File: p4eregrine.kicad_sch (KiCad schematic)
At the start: 44 parts, among them U1 ESP32-P4NRW32X, U15 TPD2EUSB30A, U3 W25Q128JVP, U7 GT-USB-7079C, Y1 Crystal_GND24

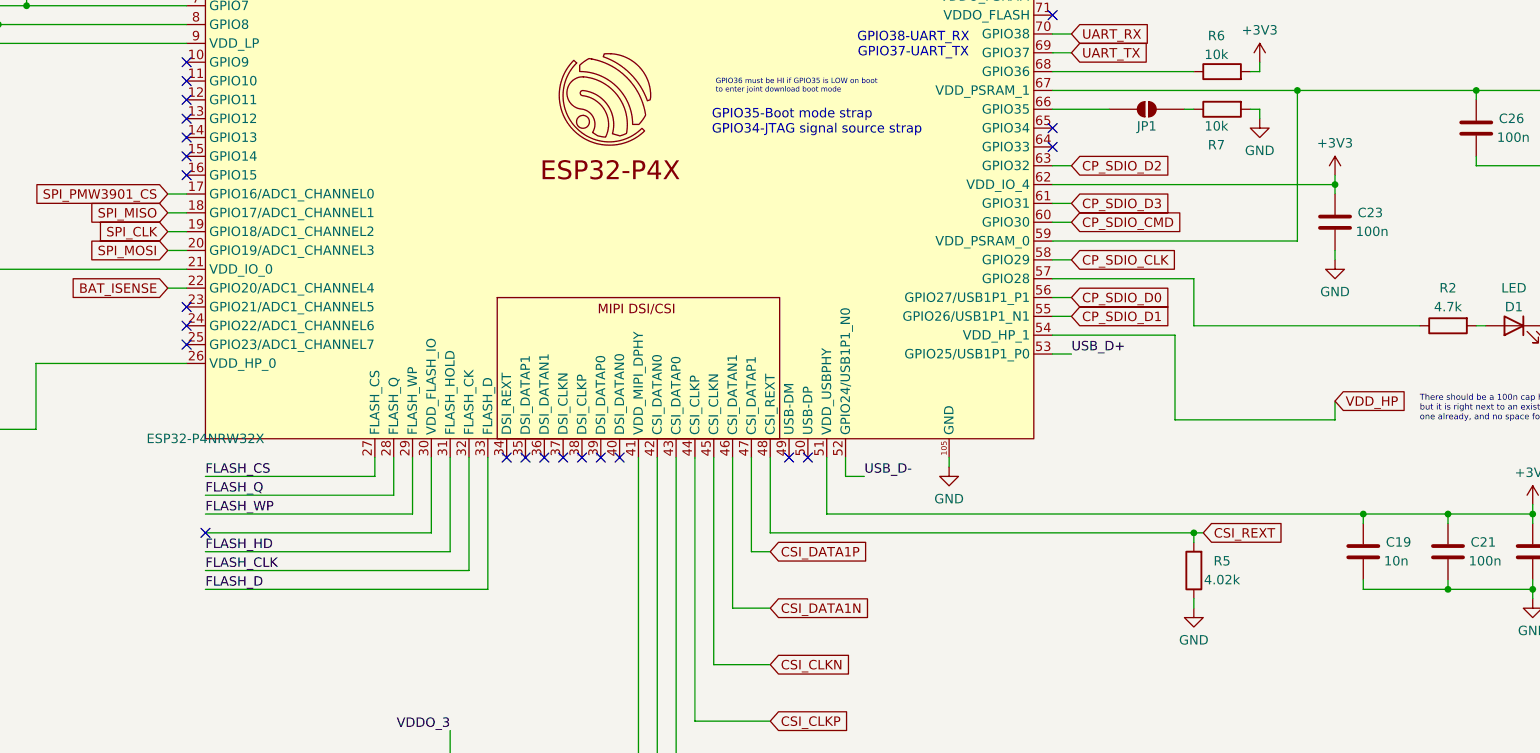
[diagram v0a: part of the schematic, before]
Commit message: Rename project
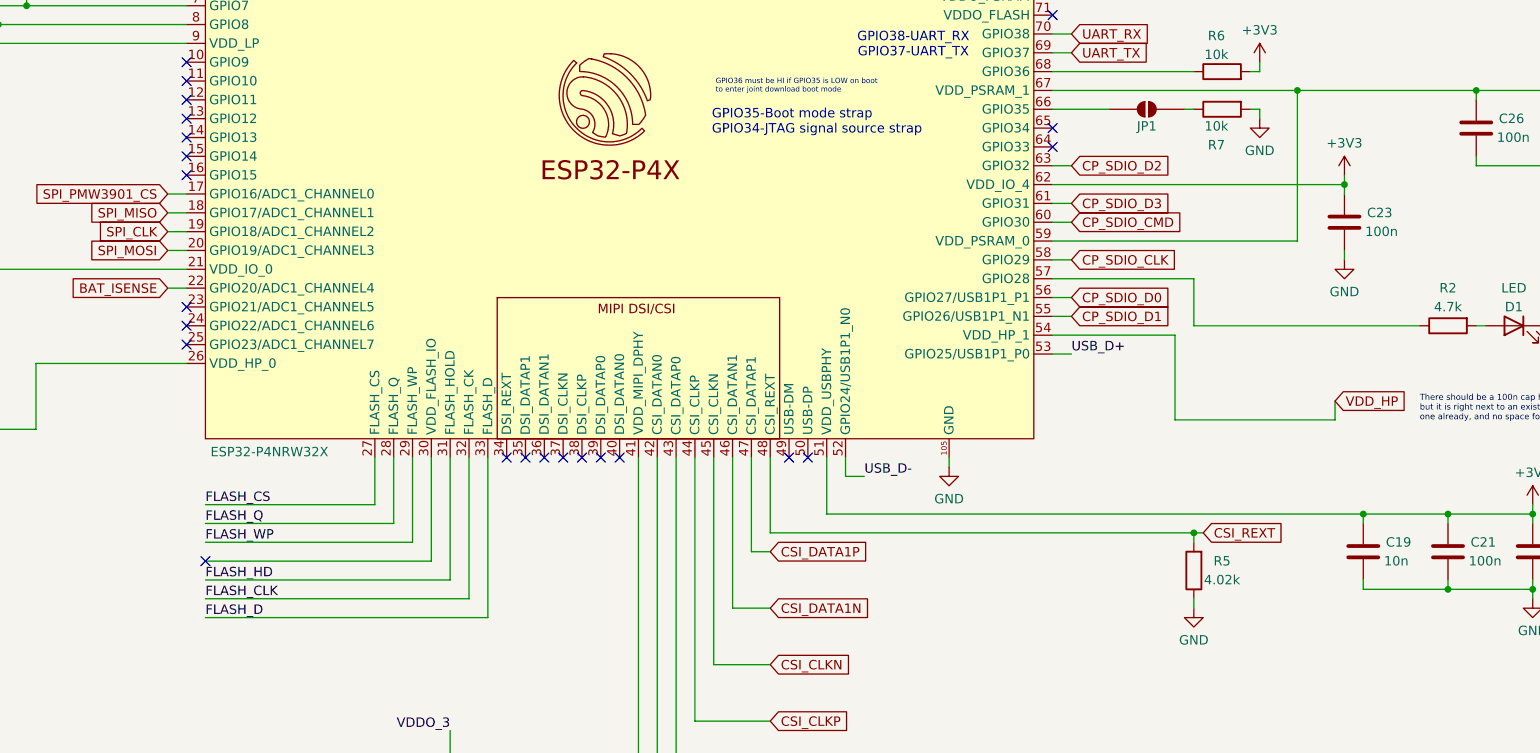
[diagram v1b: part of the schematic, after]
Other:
- title: Anticopter Duo -> P4eregrine
- moved on the sheet: C23

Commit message: Improve silkscreen and ground pour via stitching
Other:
- note added: "MIPI PHY supply"
- note added: "PMW3901B 2.1V supply"
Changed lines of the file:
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@@
+		)
+	)
+	(text "PMW3901B 2.1V supply"
+		(exclude_from_sim no)
+		(at 308.356 138.684 0)
+		(effects
+			(font
+				(size 1.27 1.27)
+			)
 		)
 	)
@@
 		(effects
 			(font
+				(size 1.27 1.27)
+			)
+		)
+	)
+	(text "MIPI PHY supply"
+		(exclude_from_sim no)
+		(at 282.702 138.176 0)
+		(effects
+			(font

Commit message: Add power supply comments to schematic
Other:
- note added: "Using 4.7k resistors to minimize BOM which is still within USB-C specs"
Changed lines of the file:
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@@
+		)
+	)
+	(text "Using 4.7k resistors to minimize BOM\nwhich is still within USB-C specs"
+		(exclude_from_sim no)
+		(at 261.112 84.074 0)
+		(effects
+			(font
+				(size 1.27 1.27)
+			)
+			(justify left)
 		)
 	)

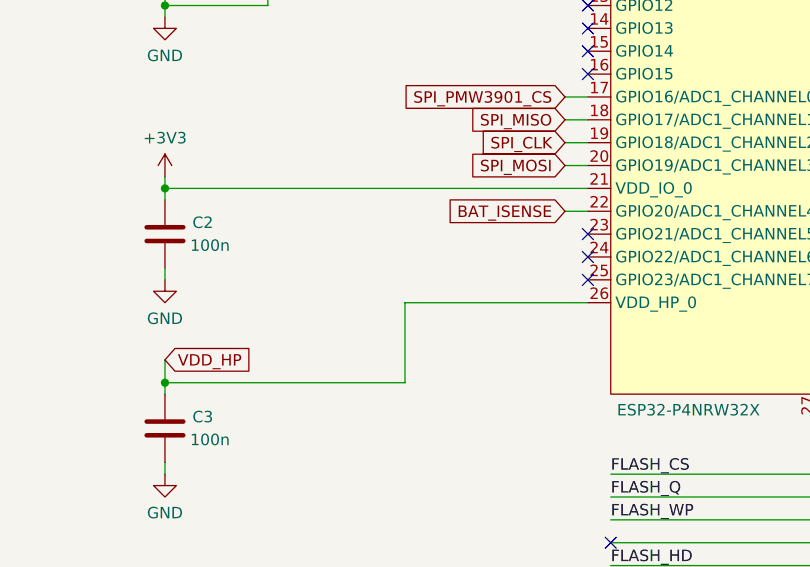
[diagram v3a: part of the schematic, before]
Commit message: Add BAT_ISENSE filtering cap and improve 3v3 plane continuity
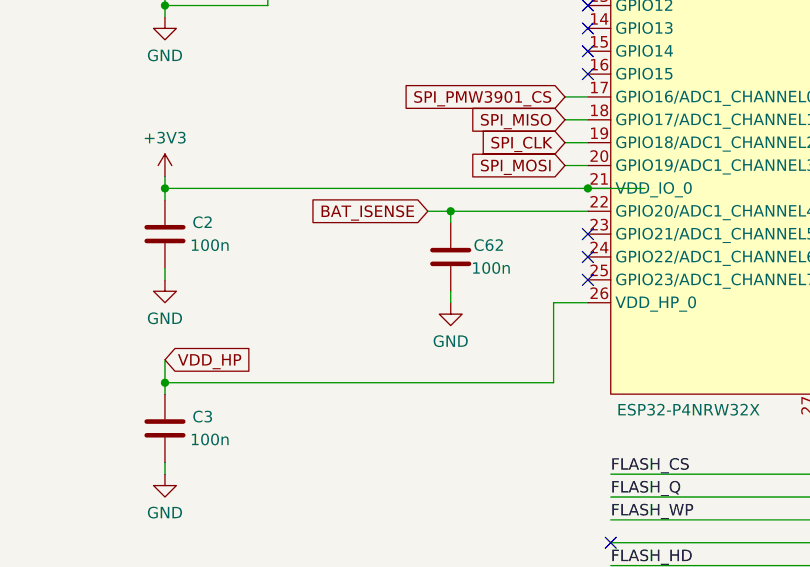
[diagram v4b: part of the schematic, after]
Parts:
- added C62: 100n, Capacitor_SMD:C_0201_0603Metric, symbol Device:C
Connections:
- net BAT_ISENSE: now also C62.1
- net GND: now also C62.2

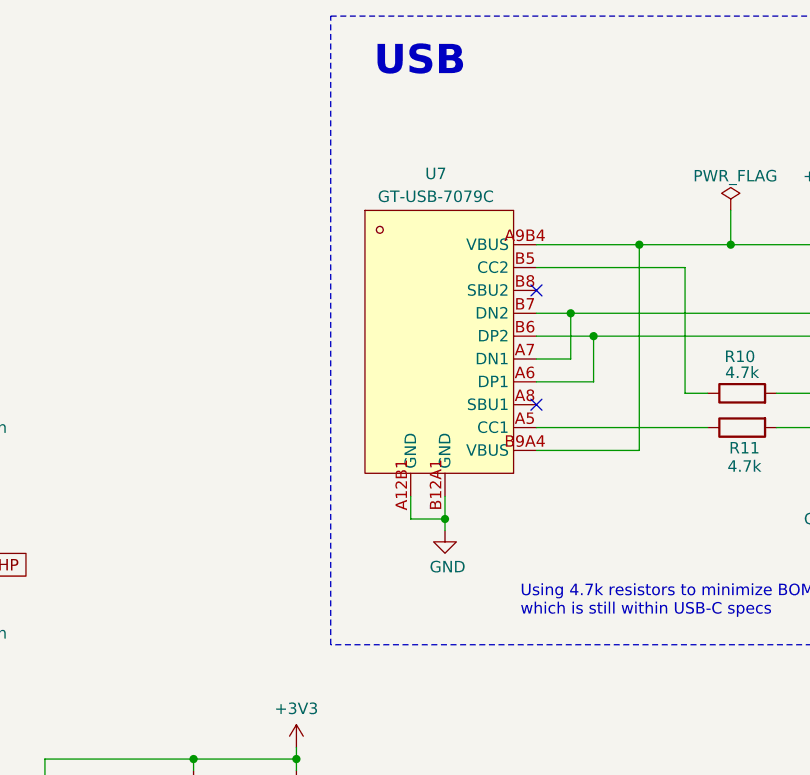
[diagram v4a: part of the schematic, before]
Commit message: Switch to a better USB-C connector
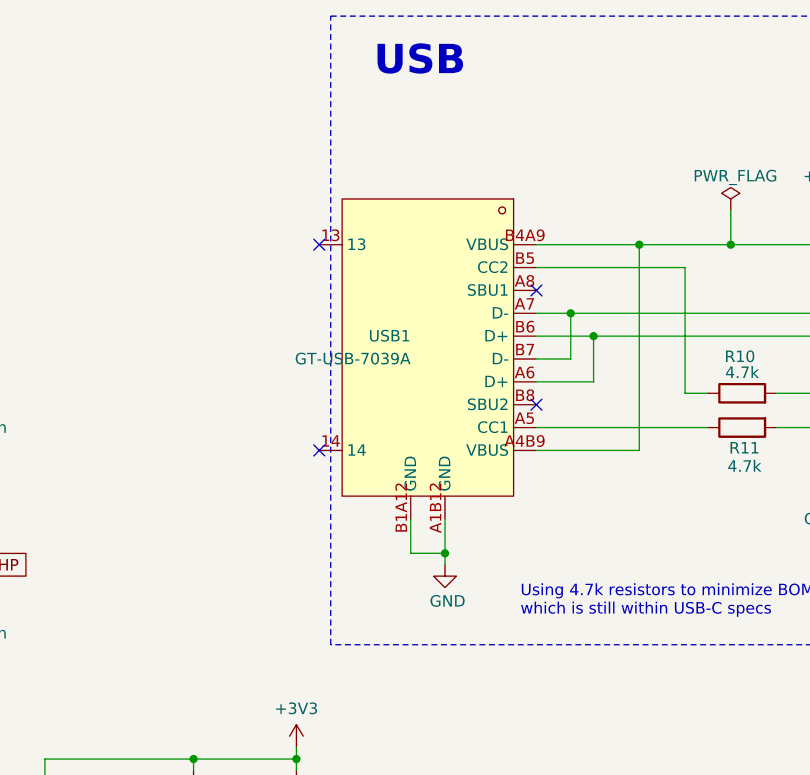
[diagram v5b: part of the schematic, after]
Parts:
- removed U7: GT-USB-7079C, easyeda2kicad:TYPE-C-SMD_GT-USB-7079C, symbol easyeda2kicad:GT-USB-7079C
- added USB1: GT-USB-7039A, easyeda2kicad:USB-C-SMD_GT-USB-7039A, symbol easyeda2kicad:GT-USB-7039A
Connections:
- net +5V: now also USB1.A4B9 (VBUS), USB1.B4A9 (VBUS)
- net GND: now also USB1.A1B12 (GND), USB1.B1A12 (GND)
- net USB_D+: now also USB1.A6 (D+), USB1.B6 (D+)
- net USB_D-: now also USB1.A7 (D-), USB1.B7 (D-)
- net at R10.1: now also USB1.B5 (CC2)
- net at R11.1: now also USB1.A5 (CC1)
- no-connect marks 42 -> 44
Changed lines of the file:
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@@
 	)
 	(junction
-		(at 252.73 74.93)
+		(at 252.73 78.74)
 		(diameter 0)
 		(color 0 0 0 0)
@@
 	)
 	(no_connect
+		(at 238.76 44.45)
+	)
+	(no_connect
 		(at 73.66 172.72)
 	)
@@
 	)
 	(no_connect
+		(at 262.89 62.23)
+	)
+	(no_connect
 		(at 73.66 198.12)
 	)
@@
 	)
 	(no_connect
-		(at 99.06 124.46)
+		(at 262.89 49.53)
 	)
 	(no_connect
-		(at 262.89 62.23)
+		(at 99.06 124.46)
 	)
 	(no_connect
@@
 	)
 	(no_connect
-		(at 262.89 49.53)
-	)
-	(no_connect
 		(at 73.66 144.78)
 	)
@@
 	)
 	(no_connect
+		(at 238.76 67.31)
+	)
+	(no_connect
 		(at 73.66 193.04)
 	)
@@
 	(wire
 		(pts
-			(xy 109.22 69.85) (xy 109.22 124.46)
+			(xy 248.92 74.93) (xy 248.92 78.74)
 		)
 		(stroke
@@
 	(wire
 		(pts
-			(xy 372.11 71.12) (xy 372.11 72.39)
+			(xy 109.22 69.85) (xy 109.22 124.46)
 		)
 		(stroke
@@
 	(wire
 		(pts
-			(xy 247.65 173.99) (xy 259.08 173.99)
+			(xy 372.11 71.12) (xy 372.11 72.39)
 		)
 		(stroke
@@
 	(wire
 		(pts
-			(xy 134.62 213.36) (xy 134.62 254)
+			(xy 247.65 173.99) (xy 259.08 173.99)
 		)
 		(stroke
@@
 	(wire
 		(pts
-			(xy 248.92 72.39) (xy 248.92 74.93)
+			(xy 134.62 213.36) (xy 134.62 254)
 		)
 		(stroke
@@
 	(wire
 		(pts
+			(xy 252.73 74.93) (xy 252.73 78.74)
+		)
+		(stroke
+			(width 0)
+			(type default)
+		)
+	)
+	(wire
+		(pts
 			(xy 118.11 58.42) (xy 118.11 59.69)
 		)
@@
 	(wire
 		(pts
-			(xy 248.92 74.93) (xy 252.73 74.93)
+			(xy 248.92 78.74) (xy 252.73 78.74)
 		)
 		(stroke
@@
 	(wire
 		(pts
-			(xy 252.73 74.93) (xy 252.73 72.39)
-		)
-		(stroke
-			(width 0)
-			(type default)
-		)
-	)
-	(wire
-		(pts
 			(xy 190.5 135.89) (xy 191.77 135.89)
 		)
@@
 	(wire
 		(pts
-			(xy 252.73 74.93) (xy 252.73 76.2)
+			(xy 252.73 78.74) (xy 252.73 80.01)
 		)
 		(stroke
@@
 	)
 	(symbol
+		(lib_id "easyeda2kicad:GT-USB-7039A")
+		(at 259.08 55.88 0)
+		(mirror y)
+		(unit 1)
+		(body_style 1)
+		(exclude_from_sim no)
+		(in_bom yes)
+		(on_board yes)
+		(in_pos_files yes)
+		(dnp no)
+		(fields_autoplaced yes)
+		(property "Reference" "USB1"
+			(at 248.92 54.6099 0)
+			(show_name no)
+			(do_not_autoplace no)
+			(effects
+				(font
+					(size 1.27 1.27)
+				)
+				(justify left)
+			)
+		)
+		(property "Value" "GT-USB-7039A"
+			(at 248.92 57.1499 0)
+			(show_name no)
+			(do_not_autoplace no)
+			(effects
+				(font
+					(size 1.27 1.27)
+				)
+				(justify left)
+			)
+		)
+		(property "Footprint" "easyeda2kicad:USB-C-SMD_GT-USB-7039A"
+			(at 259.08 82.55 0)
+			(hide yes)
+			(show_name no)
+			(do_not_autoplace no)
+			(effects
+				(font
+					(size 1.27 1.27)
+				)
+			)
+		)
+		(property "Datasheet" "https://www.lcsc.com/datasheet/C48996277.pdf"
+			(at 259.08 85.09 0)
+			(hide yes)
+			(show_name no)
+			(do_not_autoplace no)
+			(effects
+				(font
+					(size 1.27 1.27)
+				)
+			)
+		)
+		(property "Description" ""
+			(at 259.08 55.88 0)
+			(hide yes)
+			(show_name no)
+			(do_not_autoplace no)
+			(effects
+				(font
+					(size 1.27 1.27)
+				)
+			)
+		)
+		(property "Manufacturer" "G-Switch(品赞)"
+			(at 259.08 87.63 0)
+			(hide yes)
+			(show_name no)
+			(do_not_autoplace no)
+			(effects
+				(font
+					(size 1.27 1.27)
+				)
+			)
+		)
+		(property "MPN" "GT-USB-7039A"
+			(at 259.08 90.17 0)
+			(hide yes)
+			(show_name no)
+			(do_not_autoplace no)
+			(effects
+				(font
+					(size 1.27 1.27)
+				)
+			)
+		)
+		(property "LCSC Part" "C48996277"
+			(at 259.08 92.71 0)
+			(hide yes)
+			(show_name no)
+			(do_not_autoplace no)
+			(effects
+				(font
+					(size 1.27 1.27)
+				)
+			)
+		)
+		(pin "B8"
+		)
+		(pin "A7"
+		)
+		(pin "A6"
+		)
+		(pin "A5"
+		)
+		(pin "B5"
+		)
+		(pin "B6"
+		)
+		(pin "A8"
+		)
+		(pin "B1A12"
+		)
+		(pin "B7"
+		)
+		(pin "B4A9"
+		)
+		(pin "A4B9"
+		)
+		(pin "A1B12"
+		)
+		(pin "14"
+		)
+		(pin "13"
+		)
+		(instances
+			(project "p4eregrine"
+				(path "/6e047eb1-70b3-49d8-916c-92a2df32e839"
+					(reference "USB1")
+					(unit 1)
+				)
+			)
+		)
+	)
+	(symbol
 		(lib_id "power:+3V3")
 		(at 196.85 57.15 0)
@@
 	)
 	(symbol
-		(lib_id "easyeda2kicad:GT-USB-7079C")
-		(at 248.92 60.96 0)
-		(unit 1)
-		(body_style 1)
-		(exclude_from_sim no)
-		(in_bom yes)
-		(on_board yes)
-		(in_pos_files yes)
-		(dnp no)
-		(property "Reference" "U7"
-			(at 251.714 36.576 0)
-			(show_name no)
-			(do_not_autoplace no)
-			(effects
-				(font
-					(size 1.27 1.27)
-				)
-			)
-		)
-		(property "Value" "GT-USB-7079C"
-			(at 251.714 39.116 0)
-			(show_name no)
-			(do_not_autoplace no)
-			(effects
-				(font
-					(size 1.27 1.27)
-				)
-			)
-		)
-		(property "Footprint" "easyeda2kicad:TYPE-C-SMD_GT-USB-7079C"
-			(at 248.92 80.01 0)
-			(hide yes)
-			(show_name no)
-			(do_not_autoplace no)
-			(effects
-				(font
-					(size 1.27 1.27)
-				)
-			)
-		)
-		(property "Datasheet" "https://www.lcsc.com/datasheet/C5368937.pdf"
-			(at 248.92 82.55 0)
-			(hide yes)
-			(show_name no)
-			(do_not_autoplace no)
-			(effects
-				(font
-					(size 1.27 1.27)
-				)
-			)
-		)
-		(property "Description" ""
-			(at 248.92 60.96 0)
-			(hide yes)
-			(show_name no)
-			(do_not_autoplace no)
-			(effects
-				(font
-					(size 1.27 1.27)
-				)
-			)
-		)
-		(property "Manufacturer" "G-Switch(品赞)"
-			(at 248.92 85.09 0)
-			(hide yes)
-			(show_name no)
-			(do_not_autoplace no)
-			(effects
-				(font
-					(size 1.27 1.27)
-				)
-			)
-		)
-		(property "MPN" "GT-USB-7079C"
-			(at 248.92 87.63 0)
-			(hide yes)
-			(show_name no)
-			(do_not_autoplace no)
-			(effects
-				(font
-					(size 1.27 1.27)
-				)
-			)
-		)
-		(property "LCSC Part" "C5368937"
-			(at 248.92 90.17 0)
-			(hide yes)
-			(show_name no)
-			(do_not_autoplace no)
-			(effects
-				(font
-					(size 1.27 1.27)
-				)
-			)
-		)
-		(property "KLC_S3.3" ""
-			(at 248.92 60.96 0)
-			(hide yes)
-			(show_name no)
-			(do_not_autoplace no)
-			(effects
-				(font
-					(size 1.27 1.27)
-				)
-			)
-		)
-		(property "KLC_S4.1" ""
-			(at 248.92 60.96 0)
-			(hide yes)
-			(show_name no)
-			(do_not_autoplace no)
-			(effects
-				(font
-					(size 1.27 1.27)
-				)
-			)
-		)
-		(property "KLC_S5.1" ""
-			(at 248.92 60.96 0)
-			(hide yes)
-			(show_name no)
-			(do_not_autoplace no)
-			(effects
-				(font
-					(size 1.27 1.27)
-				)
-			)
-		)
-		(pin "B7"
-		)
-		(pin "B6"
-		)
-		(pin "B12A1"
-		)
-		(pin "A12B1"
-		)
-		(pin "A8"
-		)
-		(pin "B8"
-		)
-		(pin "B5"
-		)
-		(pin "B9A4"
-		)
-		(pin "A5"
-		)
-		(pin "A9B4"
-		)
-		(pin "A6"
-		)
-		(pin "A7"
-		)
-		(instances
-			(project "p4eregrine"
-				(path "/6e047eb1-70b3-49d8-916c-92a2df32e839"
-					(reference "U7")
-					(unit 1)
-				)
-			)
-		)
-	)
-	(symbol
 		(lib_id "Device:C")
 		(at 283.21 158.75 0)
@@
 	(symbol
 		(lib_id "power:GND")
-		(at 252.73 76.2 0)
+		(at 252.73 80.01 0)
 		(unit 1)
 		(body_style 1)
@@
 		(dnp no)
 		(property "Reference" "#PWR043"
-			(at 252.73 82.55 0)
+			(at 252.73 86.36 0)
 			(hide yes)
 			(show_name no)
@@
 		)
 		(property "Value" "GND"
-			(at 255.016 80.264 0)
+			(at 255.016 84.074 0)
 			(show_name no)
 			(do_not_autoplace no)
@@
 		)
 		(property "Footprint" ""
-			(at 252.73 76.2 0)
+			(at 252.73 80.01 0)
 			(hide yes)
 			(show_name no)
@@
 		)
 		(property "Datasheet" ""
-			(at 252.73 76.2 0)
+			(at 252.73 80.01 0)
 			(hide yes)
 			(show_name no)
@@
 		)
 		(property "Description" "Power symbol creates a global label with name \"GND\" , ground"
-			(at 252.73 76.2 0)
+			(at 252.73 80.01 0)
 			(hide yes)
 			(show_name no)
